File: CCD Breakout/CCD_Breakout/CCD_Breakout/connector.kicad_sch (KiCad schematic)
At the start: 3 parts

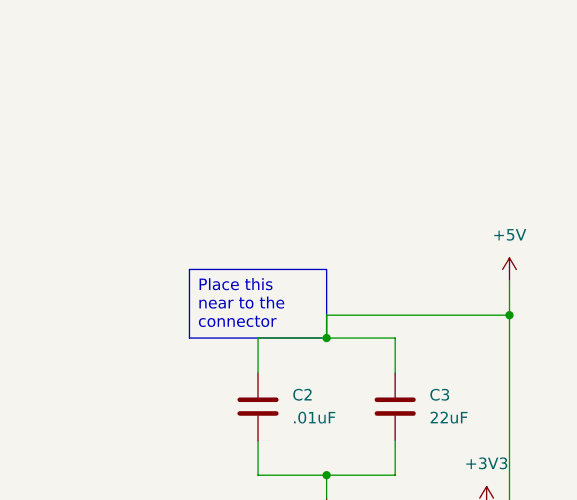
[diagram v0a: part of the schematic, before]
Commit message: OP amp filtered
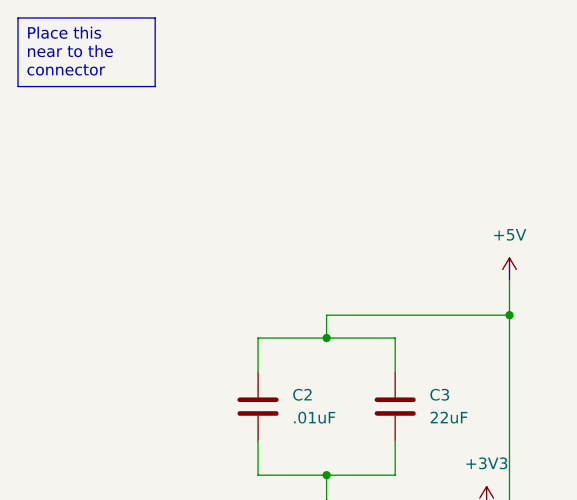
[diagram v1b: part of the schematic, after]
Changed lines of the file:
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@@
 	(text_box "Place this near to the connector"
 		(exclude_from_sim no)
-		(at 114.3 60.96 0)
+		(at 95.25 33.02 0)
 		(size 15.24 7.62)
 		(margins 0.9525 0.9525 0.9525 0.9525)

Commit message: Fix Layout Issues
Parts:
- Conn1: footprint (none) -> MRDT_Connectors:MOLEX_SL_08_Horizontal
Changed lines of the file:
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@@
 			)
 		)
-		(property "Footprint" ""
+		(property "Footprint" "MRDT_Connectors:MOLEX_SL_08_Horizontal"
 			(at 157.48 104.14 0)
 			(effects

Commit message: Initial layout
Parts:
- Conn1: footprint MRDT_Connectors:MOLEX_SL_08_Horizontal -> MRDT_Connectors:MOLEX_SL_08_Vertical
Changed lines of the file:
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@@
 			)
 		)
-		(property "Footprint" "MRDT_Connectors:MOLEX_SL_08_Horizontal"
+		(property "Footprint" "MRDT_Connectors:MOLEX_SL_08_Vertical"
 			(at 157.48 104.14 0)
 			(effects

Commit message: Fix a couple of traces and do final check
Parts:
- added Q1, Q2: SI01P10-TP, CCD:SOT-23_MCC-L, symbol RamanSpectrometerBoard:SI01P10-TP
- added R10, R11: 1k, Resistor_SMD:R_0603_1608Metric_Pad0.98x0.95mm_HandSolder, symbol Device:R
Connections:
- net +3V3: now also Q1.2 (S); no longer Conn1.1
- net +5V: now also Q2.3 (D); no longer Conn1.2
- net GND: now also R10.2, R11.2
- new net: Conn1.1, Q1.3 (D)
- new net: Conn1.2, Q2.2 (S)
- new net: Q1.1 (G), R11.1
- new net: Q2.1 (G), R10.1
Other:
- moved on the sheet: C2, C3

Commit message: Rev2 Push
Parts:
- removed Conn1: Molex_SL_08, MRDT_Connectors:MOLEX_SL_08_Vertical, symbol MRDT_Connectors:Molex_SL_08
- added Conn1: Molex_SL_10, MRDT_Connectors:MOLEX_SL_10_Vertical, symbol MRDT_Connectors:Molex_SL_10
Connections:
- net CLK: now also Conn1.4
- net CLK2: now also Conn1.7
- net GND: now also Conn1.10
- net IN: now also Conn1.3
- net ST: now also Conn1.6
- net at Q1.3 (D): now also Conn1.1
- net at Q2.2 (S): now also Conn1.2
- new net SDI: Conn1.8
- new net Trig: Conn1.5
- new net Trix_EX: Conn1.9
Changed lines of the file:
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@@
 		(color 0 0 0 0)
 	)
+	(bus_entry
+		(at 106.68 143.51)
+		(size 2.54 2.54)
+		(stroke
+			(width 0)
+			(type default)
+		)
+	)
 	(wire
 		(pts
@@
 	(wire
 		(pts
-			(xy 152.4 110.49) (xy 149.86 110.49)
+			(xy 149.86 118.11) (xy 149.86 115.57)
 		)
 		(stroke
@@
 	(wire
 		(pts
+			(xy 149.86 110.49) (xy 152.4 110.49)
+		)
+		(stroke
+			(width 0)
+			(type default)
+		)
+	)
+	(wire
+		(pts
 			(xy 93.98 54.61) (xy 93.98 62.23)
 		)
@@
 	(wire
 		(pts
-			(xy 149.86 110.49) (xy 149.86 115.57)
-		)
-		(stroke
-			(width 0)
-			(type default)
-		)
-	)
-	(wire
-		(pts
 			(xy 149.86 102.87) (xy 152.4 102.87)
 		)
@@
 	(wire
 		(pts
+			(xy 149.86 113.03) (xy 152.4 113.03)
+		)
+		(stroke
+			(width 0)
+			(type default)
+		)
+	)
+	(wire
+		(pts
 			(xy 116.84 88.9) (xy 116.84 92.71)
 		)
@@
 		(pts
 			(xy 149.86 62.23) (xy 149.86 95.25)
+		)
+		(stroke
+			(width 0)
+			(type default)
+		)
+	)
+	(wire
+		(pts
+			(xy 149.86 115.57) (xy 152.4 115.57)
 		)
 		(stroke
@@
 		)
 	)
+	(hierarchical_label "Trix_EX"
+		(shape output)
+		(at 149.86 113.03 180)
+		(effects
+			(font
+				(size 1.27 1.27)
+			)
+			(justify right)
+		)
+	)
 	(hierarchical_label "ST"
 		(shape output)
@@
 		)
 	)
-	(hierarchical_label "EOS"
+	(hierarchical_label "Trig"
 		(shape input)
 		(at 149.86 102.87 180)
@@
 		(shape output)
 		(at 149.86 100.33 180)
+		(effects
+			(font
+				(size 1.27 1.27)
+			)
+			(justify right)
+		)
+	)
+	(hierarchical_label "SDI"
+		(shape output)
+		(at 149.86 110.49 180)
 		(effects
 			(font
@@
 	(symbol
 		(lib_id "power:GND")
-		(at 149.86 115.57 0)
+		(at 149.86 118.11 0)
 		(unit 1)
 		(exclude_from_sim no)
@@
 		(fields_autoplaced yes)
 		(property "Reference" "#PWR09"
-			(at 149.86 121.92 0)
+			(at 149.86 124.46 0)
 			(effects
 				(font
@@
 		)
 		(property "Value" "GND"
-			(at 149.86 120.65 0)
+			(at 149.86 123.19 0)
 			(effects
 				(font
@@
 		)
 		(property "Footprint" ""
-			(at 149.86 115.57 0)
+			(at 149.86 118.11 0)
 			(effects
 				(font
@@
 		)
 		(property "Datasheet" ""
-			(at 149.86 115.57 0)
+			(at 149.86 118.11 0)
 			(effects
 				(font
@@
 		)
 		(property "Description" "Power symbol creates a global label with name \"GND\" , ground"
-			(at 149.86 115.57 0)
+			(at 149.86 118.11 0)
 			(effects
 				(font
@@
 				(path "/102965ac-29c6-4f96-94a4-d07431f6d693/dbede1ef-0855-4322-ae3b-1b9092ecc0c1"
 					(reference "#PWR09")
+					(unit 1)
+				)
+			)
+		)
+	)
+	(symbol
+		(lib_id "MRDT_Connectors:Molex_SL_10")
+		(at 157.48 116.84 0)
+		(unit 1)
+		(exclude_from_sim no)
+		(in_bom yes)
+		(on_board yes)
+		(dnp no)
+		(fields_autoplaced yes)
+		(property "Reference" "Conn1"
+			(at 161.29 102.8699 0)
+			(effects
+				(font
+					(size 1.524 1.524)
+				)
+				(justify left)
+			)
+		)
+		(property "Value" "Molex_SL_10"
+			(at 161.29 105.4099 0)
+			(effects
+				(font
+					(size 1.524 1.524)
+				)
+				(justify left)
+			)
+		)
+		(property "Footprint" "MRDT_Connectors:MOLEX_SL_10_Vertical"
+			(at 157.48 104.14 0)
+			(effects
+				(font
+					(size 1.524 1.524)
+				)
+				(hide yes)
+			)
+		)
+		(property "Datasheet" ""
+			(at 157.48 104.14 0)
+			(effects
+				(font
+					(size 1.524 1.524)
+				)
+				(hide yes)
+			)
+		)
+		(property "Description" ""
+			(at 157.48 116.84 0)
+			(effects
+				(font
+					(size 1.27 1.27)
+				)
+				(hide yes)
+			)
+		)
+		(pin "2"
+		)
+		(pin "4"
+		)
+		(pin "1"
+		)
+		(pin "5"
+		)
+		(pin "6"
+		)
+		(pin "8"
+		)
+		(pin "10"
+		)
+		(pin "7"
+		)
+		(pin "9"
+		)
+		(pin "3"
+		)
+		(instances
+			(project ""
+				(path "/102965ac-29c6-4f96-94a4-d07431f6d693/dbede1ef-0855-4322-ae3b-1b9092ecc0c1"
+					(reference "Conn1")
 					(unit 1)
 				)
@@
 	)
 	(symbol
-		(lib_id "MRDT_Connectors:Molex_SL_08")
-		(at 157.48 111.76 0)
-		(unit 1)
-		(exclude_from_sim no)
-		(in_bom yes)
-		(on_board yes)
-		(dnp no)
-		(fields_autoplaced yes)
-		(property "Reference" "Conn1"
-			(at 161.29 100.3299 0)
-			(effects
-				(font
-					(size 1.524 1.524)
-				)
-				(justify left)
-			)
-		)
-		(property "Value" "Molex_SL_08"
-			(at 161.29 102.8699 0)
-			(effects
-				(font
-					(size 1.524 1.524)
-				)
-				(justify left)
-			)
-		)
-		(property "Footprint" "MRDT_Connectors:MOLEX_SL_08_Vertical"
-			(at 157.48 104.14 0)
-			(effects
-				(font
-					(size 1.524 1.524)
-				)
-				(hide yes)
-			)
-		)
-		(property "Datasheet" ""
-			(at 157.48 104.14 0)
-			(effects
-				(font
-					(size 1.524 1.524)
-				)
-				(hide yes)
-			)
-		)
-		(property "Description" ""
-			(at 157.48 111.76 0)
-			(effects
-				(font
-					(size 1.27 1.27)
-				)
-				(hide yes)
-			)
-		)
-		(pin "2"
-		)
-		(pin "6"
-		)
-		(pin "5"
-		)
-		(pin "1"
-		)
-		(pin "8"
-		)
-		(pin "4"
-		)
-		(pin "7"
-		)
-		(pin "3"
-		)
-		(instances
-			(project ""
-				(path "/102965ac-29c6-4f96-94a4-d07431f6d693/dbede1ef-0855-4322-ae3b-1b9092ecc0c1"
-					(reference "Conn1")
-					(unit 1)
-				)
-			)
-		)
-	)
-	(symbol
 		(lib_id "Device:R")
 		(at 133.35 105.41 0)
@@
 		(on_board yes)
 		(dnp no)
-		(fields_autoplaced yes)
 		(property "Reference" "Q2"
 			(at 133.35 54.61 90)

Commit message: Rev 2 Layout
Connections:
- net +5V: now also Q2.2 (S); no longer Q2.3 (D)
- net at Conn1.2: now also Q2.3 (D); no longer Q2.2 (S)
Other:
- moved on the sheet: Q2
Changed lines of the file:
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@@
 	(symbol
 		(lib_id "RamanSpectrometerBoard:SI01P10-TP")
-		(at 133.35 69.85 90)
+		(at 133.35 69.85 270)
+		(mirror x)
 		(unit 1)
 		(exclude_from_sim no)
